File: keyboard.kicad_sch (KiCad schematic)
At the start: 10 parts, among them J10 KMDGX-6SG_P-S4N, U11 VT82C42, U46 74LS06

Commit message: fixed things
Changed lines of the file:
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@@
 	(wire
 		(pts
-			(xy 46.99 140.97) (xy 104.14 140.97)
-		)
-		(stroke
-			(width 0)
-			(type default)
-		)
-	)
-	(wire
-		(pts
-			(xy 91.44 102.87) (xy 106.68 102.87)
+			(xy 45.72 148.59) (xy 102.87 148.59)
+		)
+		(stroke
+			(width 0)
+			(type default)
+		)
+	)
+	(wire
+		(pts
+			(xy 91.44 102.87) (xy 105.41 102.87)
 		)
 		(stroke
@@
 	(wire
 		(pts
-			(xy 46.99 143.51) (xy 106.68 143.51)
+			(xy 45.72 156.21) (xy 105.41 156.21)
 		)
 		(stroke
@@
 	(wire
 		(pts
-			(xy 106.68 102.87) (xy 106.68 143.51)
+			(xy 105.41 102.87) (xy 105.41 156.21)
 		)
 		(stroke
@@
 	(wire
 		(pts
-			(xy 91.44 105.41) (xy 104.14 105.41)
-		)
-		(stroke
-			(width 0)
-			(type default)
-		)
-	)
-	(wire
-		(pts
-			(xy 104.14 105.41) (xy 104.14 140.97)
+			(xy 91.44 105.41) (xy 102.87 105.41)
+		)
+		(stroke
+			(width 0)
+			(type default)
+		)
+	)
+	(wire
+		(pts
+			(xy 102.87 105.41) (xy 102.87 148.59)
 		)
 		(stroke
@@
 	(hierarchical_label "MOUSE IRQ"
 		(shape input)
-		(at 46.99 140.97 180)
+		(at 45.72 148.59 180)
 		(effects
 			(font
@@
 	(hierarchical_label "KBRD IRQ"
 		(shape input)
-		(at 46.99 143.51 180)
-		(effects
-			(font
+		(at 45.72 156.21 180)
+		(effects
+			(font

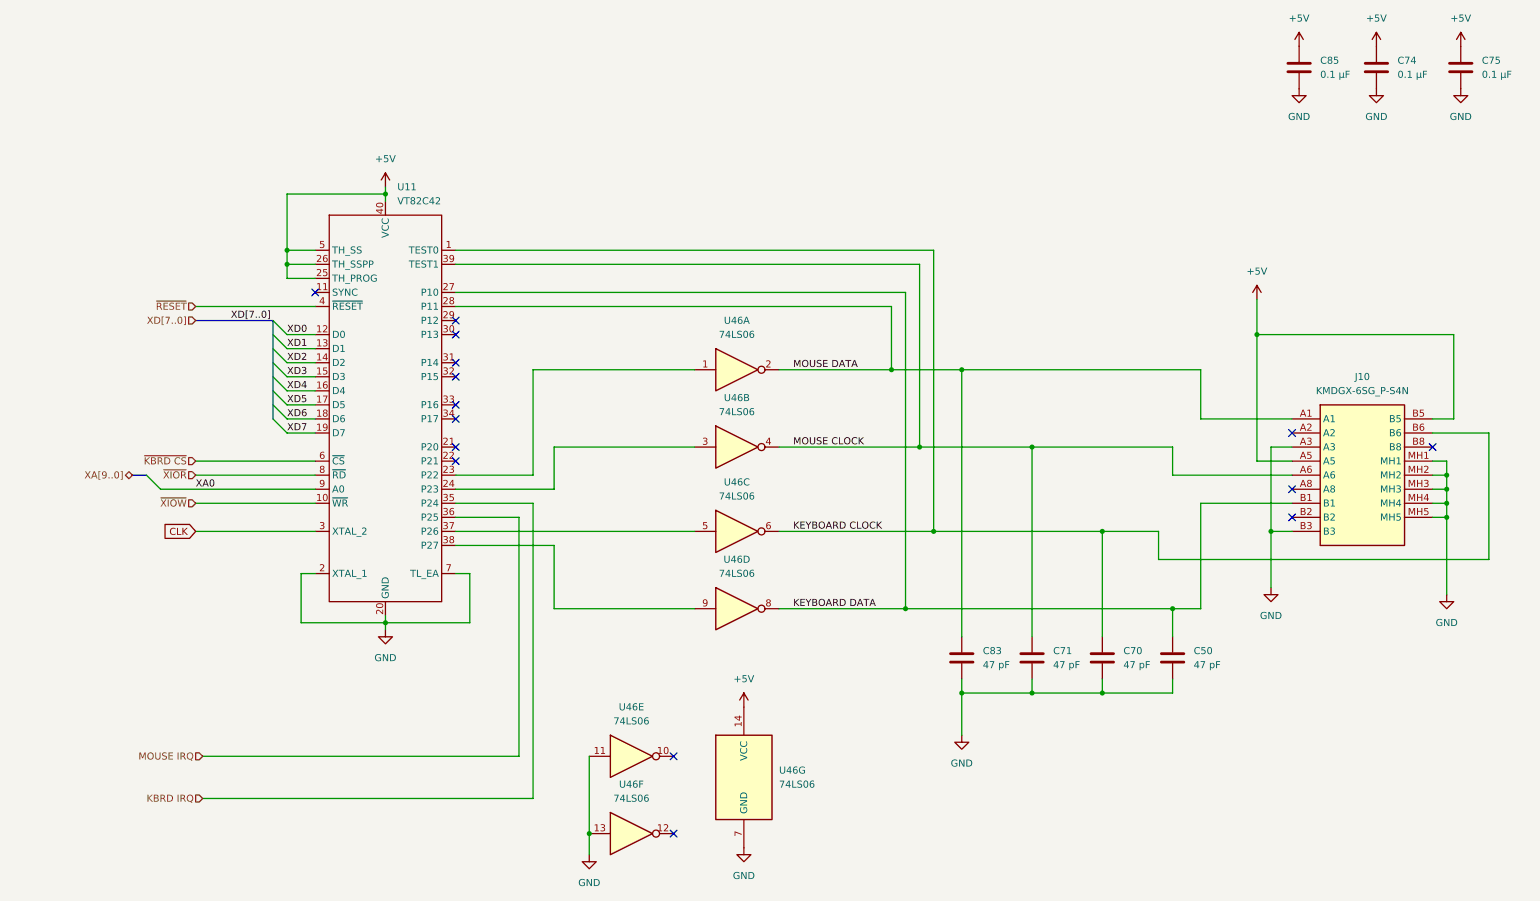
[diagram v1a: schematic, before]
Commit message: Upgraded speaker, esd protection, added dip sockets, adjusted routing
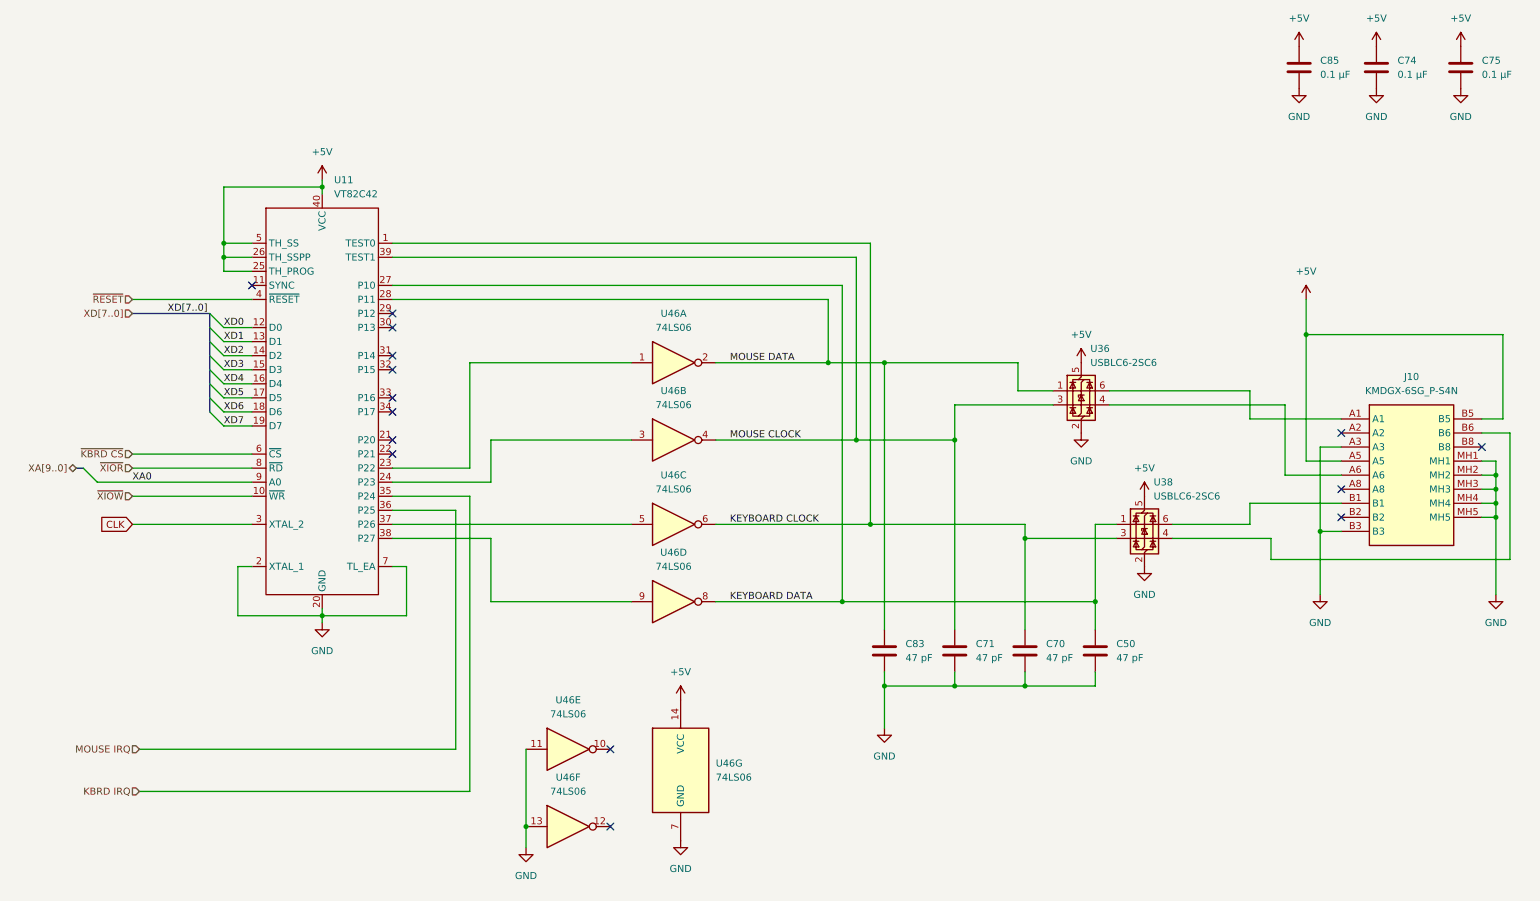
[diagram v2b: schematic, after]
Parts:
- added U36, U38: USBLC6-2SC6, Package_TO_SOT_SMD:SOT-23-6, symbol Power_Protection:USBLC6-2SC6
- U11: footprint Package_DIP:DIP-40_W15.24mm -> Package_DIP:DIP-40_W15.24mm_Socket
- U46: footprint Package_DIP:DIP-14_W7.62mm -> Package_DIP:DIP-14_W7.62mm_Socket
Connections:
- net +5V: now also U36.5 (VBUS), U38.5 (VBUS)
- net GND: now also U36.2 (GND), U38.2 (GND)
- net KEYBOARD CLOCK: now also U38.3 (I/O2); no longer J10.B6
- net KEYBOARD DATA: now also U38.1 (I/O1); no longer J10.B1
- net MOUSE CLOCK: now also U36.3 (I/O2); no longer J10.A6
- net MOUSE DATA: now also U36.1 (I/O1); no longer J10.A1
- new net: J10.A1, U36.6 (I/O1)
- new net: J10.A6, U36.4 (I/O2)
- new net: J10.B1, U38.6 (I/O1)
- new net: J10.B6, U38.4 (I/O2)
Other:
- moved on the sheet: C50, C70, C71, C83, J10, U11, U46A, U46B, U46C, U46D, U46E, U46F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

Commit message: final commit before spinning
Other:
- moved on the sheet: U38
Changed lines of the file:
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@@
 	)
 	(junction
+		(at 194.31 109.22)
+		(diameter 0)
+		(color 0 0 0 0)
+	)
+	(junction
 		(at 247.65 107.95)
 		(diameter 0)
@@
 	)
 	(junction
-		(at 194.31 109.22)
-		(diameter 0)
-		(color 0 0 0 0)
-	)
-	(junction
 		(at 181.61 91.44)
 		(diameter 0)
@@
 	(wire
 		(pts
-			(xy 220.98 109.22) (xy 238.76 109.22)
+			(xy 223.52 109.22) (xy 238.76 109.22)
 		)
 		(stroke
@@
 	(wire
 		(pts
-			(xy 234.95 106.68) (xy 220.98 106.68)
+			(xy 234.95 106.68) (xy 223.52 106.68)
 		)
 		(stroke
@@
 	(wire
 		(pts
-			(xy 194.31 109.22) (xy 210.82 109.22)
+			(xy 194.31 109.22) (xy 213.36 109.22)
 		)
 		(stroke
@@
 	(wire
 		(pts
-			(xy 207.01 106.68) (xy 210.82 106.68)
+			(xy 207.01 106.68) (xy 213.36 106.68)
 		)
 		(stroke
@@
 	(symbol
 		(lib_id "power:VCC")
-		(at 215.9 101.6 0)
+		(at 218.44 101.6 0)
 		(unit 1)
 		(body_style 1)
@@
 		(fields_autoplaced yes)
 		(property "Reference" "#PWR0101"
-			(at 215.9 105.41 0)
+			(at 218.44 105.41 0)
 			(hide yes)
 			(show_name no)
@@
 		)
 		(property "Value" "+5V"
-			(at 215.9 96.52 0)
+			(at 218.44 96.52 0)
 			(show_name no)
 			(do_not_autoplace no)
@@
 		)
 		(property "Footprint" ""
-			(at 215.9 101.6 0)
+			(at 218.44 101.6 0)
 			(hide yes)
 			(show_name no)
@@
 		)
 		(property "Datasheet" ""
-			(at 215.9 101.6 0)
+			(at 218.44 101.6 0)
 			(hide yes)
 			(show_name no)
@@
 		)
 		(property "Description" "Power symbol creates a global label with name \"VCC\""
-			(at 215.9 101.6 0)
+			(at 218.44 101.6 0)
 			(hide yes)
 			(show_name no)
@@
 	(symbol
 		(lib_id "power:GND")
-		(at 215.9 114.3 0)
+		(at 218.44 114.3 0)
 		(unit 1)
 		(body_style 1)
@@
 		(fields_autoplaced yes)
 		(property "Reference" "#PWR0168"
-			(at 215.9 120.65 0)
+			(at 218.44 120.65 0)
 			(hide yes)
 			(show_name no)
@@
 		)
 		(property "Value" "GND"
-			(at 215.9 119.38 0)
+			(at 218.44 119.38 0)
 			(show_name no)
 			(do_not_autoplace no)
@@
 		)
 		(property "Footprint" ""
-			(at 215.9 114.3 0)
+			(at 218.44 114.3 0)
 			(hide yes)
 			(show_name no)
@@
 		)
 		(property "Datasheet" ""
-			(at 215.9 114.3 0)
+			(at 218.44 114.3 0)
 			(hide yes)
 			(show_name no)
@@
 		)
 		(property "Description" "Power symbol creates a global label with name \"GND\" , ground"
-			(at 215.9 114.3 0)
+			(at 218.44 114.3 0)
 			(hide yes)
 			(show_name no)
@@
 	(symbol
 		(lib_id "Power_Protection:USBLC6-2SC6")
-		(at 215.9 106.68 0)
+		(at 218.44 106.68 0)
 		(unit 1)
 		(body_style 1)
@@
 		(fields_autoplaced yes)
 		(property "Reference" "U38"
-			(at 217.5511 99.06 0)
+			(at 220.0911 99.06 0)
 			(show_name no)
 			(do_not_autoplace no)
@@
 		)
 		(property "Value" "USBLC6-2SC6"
-			(at 217.5511 101.6 0)
+			(at 220.0911 101.6 0)
 			(show_name no)
 			(do_not_autoplace no)
@@
 		)
 		(property "Footprint" "Package_TO_SOT_SMD:SOT-23-6"
-			(at 217.17 113.03 0)
+			(at 219.71 113.03 0)
 			(hide yes)
 			(show_name no)
@@
 		)
 		(property "Datasheet" "https://www.st.com/resource/en/datasheet/usblc6-2.pdf"
-			(at 217.17 114.935 0)
+			(at 219.71 114.935 0)
 			(hide yes)
 			(show_name no)
@@
 		)
 		(property "Description" "Very low capacitance ESD protection diode, 2 data-line, SOT-23-6"
-			(at 215.9 106.68 0)
+			(at 218.44 106.68 0)
 			(hide yes)
 			(show_name no)
